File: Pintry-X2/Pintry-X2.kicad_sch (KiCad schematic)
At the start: 0 parts

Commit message: Bunch of shit done, probably should commit
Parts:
- added FID1, FID3, FID5: FiducialTop, symbol Mechanical:Fiducial
- added FID2, FID4, FID6: FiducialBot, symbol Mechanical:Fiducial
- added H1, H2, H3, H4: M3 MountingHole, symbol Mechanical:MountingHole
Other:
- sheet CM4 renamed CM4-ETH-GPIO
- added sheet CM4-USB-PCIe (CM4-USB-PCIe.kicad_sch)
- added sheet PCIe to SATA (PCIe_To_SATA.kicad_sch)
- added sheet Power Supply (PowerSupply.kicad_sch)
- sheet CM4-ETH-GPIO: file CM4.kicad_sch -> CM4-ETH-GPIO.kicad_sch
- note added: "PCIe RX/TX from Host perspective"
- company: (none) -> www.cezarchirila.com
- title: (none) -> Pintry X2

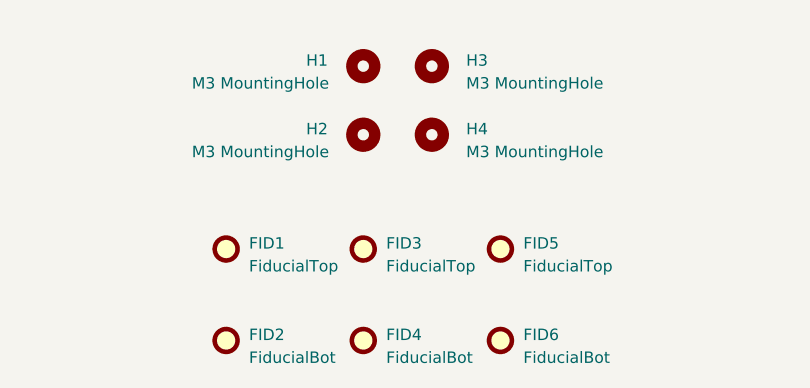
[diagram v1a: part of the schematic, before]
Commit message: Cleaned up schematic
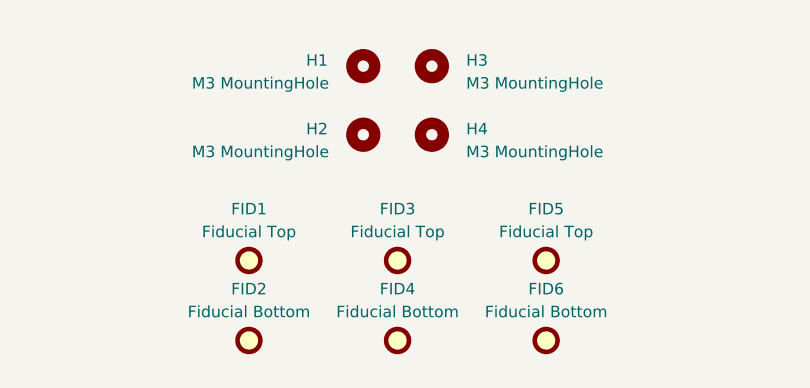
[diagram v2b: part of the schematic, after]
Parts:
- FID1, FID3, FID5: value FiducialTop -> Fiducial Top; footprint (none) -> Fiducial:Fiducial_1mm_Mask2mm; now in the parts list
- FID2, FID4, FID6: value FiducialBot -> Fiducial Bottom; footprint (none) -> Fiducial:Fiducial_1mm_Mask2mm; now in the parts list
- H1, H2, H3, H4: footprint (none) -> MountingHole:MountingHole_3.2mm_M3

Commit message: Finished Shematic. Starting PCB
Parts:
- H1, H2, H3, H4: footprint MountingHole:MountingHole_3.2mm_M3 -> PintryParts-Footprints:MountingHole_3.2mm_M3

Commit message: PCB Routing Complete - needs review
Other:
- sheet CM4-ETH-GPIO ports: added ~{RPIBOOT}; removed none
- sheet CM4-USB-PCIe ports: added ~{PCIe_RST}, ~{RPIBOOT}; removed ~PCIe_RST
- sheet PCIe to SATA ports: added ~{PCIe_RST}; removed ~PCIe_RST
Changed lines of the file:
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@@
-(kicad_sch (version 20210406) (generator eeschema)
+(kicad_sch (version 20210621) (generator eeschema)
   (paper "A3")
   (title_block
@@
     (comment 9 "${DrawnBy}")
   )
+  (wire (pts (xy 139.7 119.38) (xy 152.4 119.38))
+    (stroke (width 0) (type default) (color 0 0 0 0))
+  )
   (wire (pts (xy 190.5 96.52) (xy 203.2 96.52))
     (stroke (width 0) (type solid) (color 0 0 0 0))
@@
       (effects (font (size 1.27 1.27)) (justify left top))
     )
+    (pin "~{RPIBOOT}" input (at 139.7 119.38 0)
+      (effects (font (size 1.27 1.27)) (justify right))
+    )
   )
   (sheet (at 152.4 88.9) (size 38.1 38.1) (fields_autoplaced)
@@
       (effects (font (size 1.27 1.27)) (justify left top))
     )
-    (pin "~PCIe_RST" output (at 190.5 96.52 0)
+    (pin "~{PCIe_RST}" output (at 190.5 96.52 0)
       (effects (font (size 1.27 1.27)) (justify right))
     )
@@
     (pin "PCIe_TX_P" output (at 190.5 116.84 0)
       (effects (font (size 1.27 1.27)) (justify right))
+    )
+    (pin "~{RPIBOOT}" output (at 152.4 119.38 180)
+      (effects (font (size 1.27 1.27)) (justify left))
     )
   )
@@
       (effects (font (size 1.27 1.27)) (justify left))
     )
-    (pin "~PCIe_RST" input (at 203.2 96.52 180)
+    (pin "~{PCIe_RST}" input (at 203.2 96.52 180)
       (effects (font (size 1.27 1.27)) (justify left))
     )
@@
       (reference "#PWR0144") (unit 1) (value "GND") (footprint "")
     )
+    (path "/43f16507-298f-4d98-bfaf-f1724bb94aba/9d0fe3a6-d02b-4920-9231-813081adfc8b"
+      (reference "#PWR0145") (unit 1) (value "GND") (footprint "")
+    )
     (path "/9b6e5347-f86e-4db9-bbf5-31af483a2407/5e55dc42-0089-47bf-9024-2334ea89628c"
       (reference "#PWR0146") (unit 1) (value "GND") (footprint "")
@@
       (reference "#PWR0154") (unit 1) (value "GND") (footprint "")
     )
-    (path "/43f16507-298f-4d98-bfaf-f1724bb94aba/791d2112-1af0-4cac-90c1-821c2089ea1d"
-      (reference "#PWR0155") (unit 1) (value "GND") (footprint "")
-    )
     (path "/43f16507-298f-4d98-bfaf-f1724bb94aba/8ffb6013-907a-415f-9140-e7469dfe0209"
       (reference "#PWR0156") (unit 1) (value "GND") (footprint "")
@@
       (reference "Q2") (unit 1) (value "BSS138PW") (footprint "Package_TO_SOT_SMD:SOT-323_SC-70")
     )
+    (path "/43f16507-298f-4d98-bfaf-f1724bb94aba/81596eb1-0436-4fd2-ad41-2e3aa5c836ef"
+      (reference "Q3") (unit 1) (value "BSS138PW") (footprint "Package_TO_SOT_SMD:SOT-323_SC-70")
+    )
     (path "/9b6e5347-f86e-4db9-bbf5-31af483a2407/de22381e-32d3-41cf-bf63-26066b0511fe"
-      (reference "Q5") (unit 1) (value "SIA483DJ") (footprint "Package_TO_SOT_SMD:Vishay_PowerPAK_SC70-6L_Single")
+      (reference "Q5") (unit 1) (value "SIA483DJ") (footprint "PintryParts-Footprints:Vishay_PowerPAK_SC70-6L_Single")
     )
     (path "/9b6e5347-f86e-4db9-bbf5-31af483a2407/28421447-7a88-445b-abbf-05f73eb42385"
@@
     )
     (path "/9b6e5347-f86e-4db9-bbf5-31af483a2407/d3b4a547-7eca-4eee-b20e-40fe88c2e1c0"
-      (reference "Q7") (unit 1) (value "SIA483DJ") (footprint "Package_TO_SOT_SMD:Vishay_PowerPAK_SC70-6L_Single")
+      (reference "Q7") (unit 1) (value "SIA483DJ") (footprint "PintryParts-Footprints:Vishay_PowerPAK_SC70-6L_Single")
     )
     (path "/9d10082d-34aa-4b2a-aed1-f6a03e5ca555/359a6298-4ff1-4a7f-aed5-ce92ce328403"
@@
       (reference "R15") (unit 1) (value "100K") (footprint "PintryParts-Footprints:R_0402_1005Metric")
     )
+    (path "/43f16507-298f-4d98-bfaf-f1724bb94aba/672e95d7-1401-4782-b5cf-4656984e1abd"
+      (reference "R16") (unit 1) (value "4K7") (footprint "PintryParts-Footprints:R_0402_1005Metric")
+    )
     (path "/d684709a-a958-44ce-bda0-0bbe09272c17/ff52700d-8342-4346-a086-6f3401fcb1b4"
       (reference "R17") (unit 1) (value "4K7") (footprint "PintryParts-Footprints:R_0402_1005Metric")
@@
       (reference "R18") (unit 1) (value "4K7") (footprint "PintryParts-Footprints:R_0402_1005Metric")
     )
+    (path "/9d10082d-34aa-4b2a-aed1-f6a03e5ca555/6b228126-496c-42dc-b2d9-4dea7ae53083"
+      (reference "R19") (unit 1) (value "1K") (footprint "PintryParts-Footprints:R_0402_1005Metric")
+    )
+    (path "/9d10082d-34aa-4b2a-aed1-f6a03e5ca555/31137e12-48b1-4c0a-8c02-c20834998509"
+      (reference "R20") (unit 1) (value "1K") (footprint "PintryParts-Footprints:R_0402_1005Metric")
+    )
     (path "/d684709a-a958-44ce-bda0-0bbe09272c17/9cefef80-cbca-400d-9c9b-05546550af89"
       (reference "R21") (unit 1) (value "4K7") (footprint "PintryParts-Footprints:R_0402_1005Metric")
@@
     )
     (path "/9b6e5347-f86e-4db9-bbf5-31af483a2407/0882f70b-802c-4545-afe3-58c1fc910636"
-      (reference "TP1") (unit 1) (value "VIN") (footprint "TestPoint:TestPoint_Pad_D1.0mm")
+      (reference "TP1") (unit 1) (value "VIN") (footprint "PintryParts-Footprints:TestPoint_Pad_D1.0mm")
     )
     (path "/9b6e5347-f86e-4db9-bbf5-31af483a2407/f26086ec-723e-4c84-ab4c-4ea21b12643d"
-      (reference "TP2") (unit 1) (value "VCC") (footprint "TestPoint:TestPoint_Pad_D1.0mm")
+      (reference "TP2") (unit 1) (value "VCC") (footprint "PintryParts-Footprints:TestPoint_Pad_D1.0mm")
     )
     (path "/9b6e5347-f86e-4db9-bbf5-31af483a2407/8064058a-d19e-48ad-8198-501652b96543"
-      (reference "TP3") (unit 1) (value "VIN_RP") (footprint "TestPoint:TestPoint_Pad_D1.0mm")
+      (reference "TP3") (unit 1) (value "VIN_RP") (footprint "PintryParts-Footprints:TestPoint_Pad_D1.0mm")
     )
     (path "/9b6e5347-f86e-4db9-bbf5-31af483a2407/b4f89b4b-1bf6-4b5b-acbb-f37c37c96e6f"
-      (reference "TP4") (unit 1) (value "+5V") (footprint "TestPoint:TestPoint_Pad_D1.0mm")
+      (reference "TP4") (unit 1) (value "+5V") (footprint "PintryParts-Footprints:TestPoint_Pad_D1.0mm")
     )
     (path "/9b6e5347-f86e-4db9-bbf5-31af483a2407/2e24b85f-2f5e-4941-a948-77329a33f8fa"
-      (reference "TP5") (unit 1) (value "+12V") (footprint "TestPoint:TestPoint_Pad_D1.0mm")
+      (reference "TP5") (unit 1) (value "+12V") (footprint "PintryParts-Footprints:TestPoint_Pad_D1.0mm")
     )
     (path "/9b6e5347-f86e-4db9-bbf5-31af483a2407/83ab9e94-6dc3-42bd-ade7-a66fa1afb484"
-      (reference "TP6") (unit 1) (value "GND") (footprint "TestPoint:TestPoint_Pad_D1.0mm")
+      (reference "TP6") (unit 1) (value "GND") (footprint "PintryParts-Footprints:TestPoint_Pad_D1.0mm")
     )
     (path "/9d10082d-34aa-4b2a-aed1-f6a03e5ca555/5f06c418-35af-4a8b-8229-a1fb9d539fcb"
-      (reference "TP7") (unit 1) (value "RUN_PG") (footprint "TestPoint:TestPoint_Pad_D1.0mm")
+      (reference "TP7") (unit 1) (value "RUN_PG") (footprint "PintryParts-Footprints:TestPoint_Pad_D1.0mm")
     )
     (path "/9d10082d-34aa-4b2a-aed1-f6a03e5ca555/04199f63-e06c-4307-a8f2-2c85a7013a1a"
-      (reference "TP8") (unit 1) (value "GLOBAL_EN") (footprint "TestPoint:TestPoint_Pad_D1.0mm")
+      (reference "TP8") (unit 1) (value "GLOBAL_EN") (footprint "PintryParts-Footprints:TestPoint_Pad_D1.0mm")
     )
     (path "/9d10082d-34aa-4b2a-aed1-f6a03e5ca555/942e11b9-c098-48e4-b9a0-ea01936abccd"
-      (reference "TP9") (unit 1) (value "FAN1") (footprint "TestPoint:TestPoint_Pad_D1.0mm")
+      (reference "TP9") (unit 1) (value "FAN1") (footprint "PintryParts-Footprints:TestPoint_Pad_D1.0mm")
     )
     (path "/9d10082d-34aa-4b2a-aed1-f6a03e5ca555/d5de8427-e722-4a00-9973-3fee3858dae5"
-      (reference "TP10") (unit 1) (value "FAN0") (footprint "TestPoint:TestPoint_Pad_D1.0mm")
+      (reference "TP10") (unit 1) (value "FAN0") (footprint "PintryParts-Footprints:TestPoint_Pad_D1.0mm")
     )
     (path "/d684709a-a958-44ce-bda0-0bbe09272c17/b6d8b293-1883-4d02-93bf-609d602728ca"
-      (reference "TP11") (unit 1) (value "+1V2") (footprint "TestPoint:TestPoint_Pad_D1.0mm")
+      (reference "TP11") (unit 1) (value "+1V2") (footprint "PintryParts-Footprints:TestPoint_Pad_D1.0mm")
     )
     (path "/43f16507-298f-4d98-bfaf-f1724bb94aba/fbba102e-6543-4d65-941e-5581190f8529"
-      (reference "TP14") (unit 1) (value "VUSB") (footprint "TestPoint:TestPoint_Pad_D1.0mm")
+      (reference "TP14") (unit 1) (value "VUSB") (footprint "PintryParts-Footprints:TestPoint_Pad_D1.0mm")
     )
     (path "/9b6e5347-f86e-4db9-bbf5-31af483a2407/bdb5647d-0615-4715-bb8e-a987dc84acec"
-      (reference "TP15") (unit 1) (value "GND") (footprint "TestPoint:TestPoint_Pad_D1.0mm")
+      (reference "TP15") (unit 1) (value "GND") (footprint "PintryParts-Footprints:TestPoint_Pad_D1.0mm")
     )
     (path "/9b6e5347-f86e-4db9-bbf5-31af483a2407/8aaeecbf-c658-4df9-8c68-6792c6dc1446"
-      (reference "TP16") (unit 1) (value "GND") (footprint "TestPoint:TestPoint_Pad_D1.0mm")
+      (reference "TP16") (unit 1) (value "GND") (footprint "PintryParts-Footprints:TestPoint_Pad_D1.0mm")
     )
     (path "/9b6e5347-f86e-4db9-bbf5-31af483a2407/59f4fbe6-270b-4071-926d-f9afce828fb6"
-      (reference "TP17") (unit 1) (value "GND") (footprint "TestPoint:TestPoint_Pad_D1.0mm")
+      (reference "TP17") (unit 1) (value "GND") (footprint "PintryParts-Footprints:TestPoint_Pad_D1.0mm")
     )
     (path "/9d10082d-34aa-4b2a-aed1-f6a03e5ca555/f3b7861f-1ccf-4504-af2b-07baaa0f74c4"
-      (reference "TP18") (unit 1) (value "3V3") (footprint "TestPoint:TestPoint_Pad_D1.0mm")
+      (reference "TP18") (unit 1) (value "3V3") (footprint "PintryParts-Footprints:TestPoint_Pad_D1.0mm")
     )
     (path "/9d10082d-34aa-4b2a-aed1-f6a03e5ca555/0fed7a6b-5f61-431f-abc4-a9bf842b3eee"

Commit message: Updated to Rev 1.1. Added interactive HTML
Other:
- note added: "Changelog:"
- note added: "V1.0 - Initial Release"
- note added: "V1.1 - Changed R14 to 1K. Fixed SST25VF512A footprint. Fixed Y1 pinout."
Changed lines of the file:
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@@
     (stroke (width 0) (type solid) (color 0 0 0 0))
+  )
+  (text "Changelog:\n" (at 38.1 238.76 0)
+    (effects (font (size 1.8 1.8) (thickness 0.254) bold) (justify left bottom))
+  )
+  (text "V1.0 - Initial Release\n" (at 38.1 242.57 0)
+    (effects (font (size 1.8 1.8)) (justify left bottom))
+  )
+  (text "V1.1 - Changed R14 to 1K. Fixed SST25VF512A footprint. Fixed Y1 pinout.\n\n\n\n "
+    (at 38.1 257.81 0)
+    (effects (font (size 1.8 1.8)) (justify left bottom))
   )
   (text "PCIe RX/TX from Host perspective" (at 179.07 133.35 0)
@@
     )
     (path "/d684709a-a958-44ce-bda0-0bbe09272c17/4b139e0e-b32a-4583-81cf-842901f3e977"
-      (reference "R14") (unit 1) (value "4K7") (footprint "PintryParts-Footprints:R_0402_1005Metric")
+      (reference "R14") (unit 1) (value "1K") (footprint "PintryParts-Footprints:R_0402_1005Metric")
     )
     (path "/9d10082d-34aa-4b2a-aed1-f6a03e5ca555/9740a87c-eb70-42e8-8352-c46b996b0405"
@@
     )
     (path "/d684709a-a958-44ce-bda0-0bbe09272c17/0d7ef888-f0d3-4c0a-9db1-a1092ada64a7"
-      (reference "U10") (unit 1) (value "SST25VF512A") (footprint "Package_SO:SOIC-8_5.275x5.275mm_P1.27mm")
+      (reference "U10") (unit 1) (value "SST25VF512A") (footprint "Package_SO:SOIC-8_3.9x4.9mm_P1.27mm")
     )
     (path "/d684709a-a958-44ce-bda0-0bbe09272c17/967707d1-cc15-44c4-ad21-402dd30edde5"

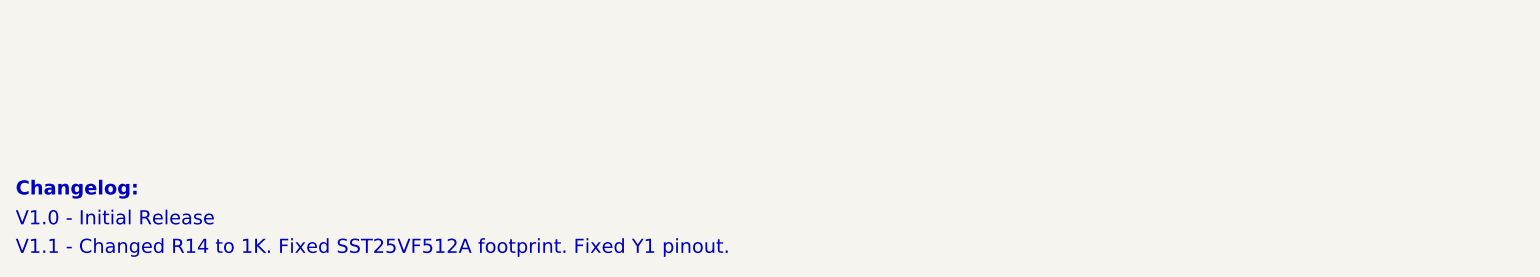
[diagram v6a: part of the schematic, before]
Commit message: Fixed ON/OFF Button
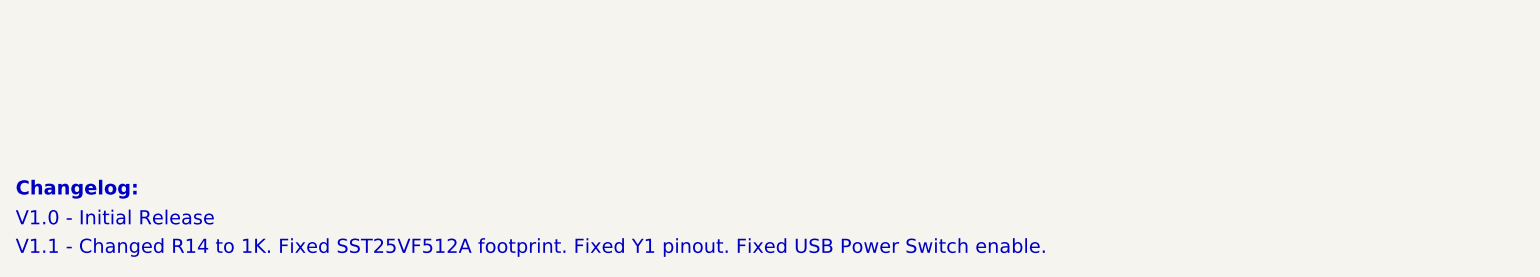
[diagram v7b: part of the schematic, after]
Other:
- note added: "V1.1 - Changed R14 to 1K. Fixed SST25VF512A footprint. Fixed Y1 pinout. Fixed USB Power Switch enable."
- note removed: "V1.1 - Changed R14 to 1K. Fixed SST25VF512A footprint. Fixed Y1 pinout."
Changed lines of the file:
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@@
     (effects (font (size 1.8 1.8)) (justify left bottom))
   )
-  (text "V1.1 - Changed R14 to 1K. Fixed SST25VF512A footprint. Fixed Y1 pinout.\n\n\n\n "
+  (text "V1.1 - Changed R14 to 1K. Fixed SST25VF512A footprint. Fixed Y1 pinout. Fixed USB Power Switch enable. \n\n\n\n "
     (at 38.1 257.81 0)
     (effects (font (size 1.8 1.8)) (justify left bottom))
@@
       (reference "#PWR033") (unit 1) (value "+3.3V") (footprint "")
     )
-    (path "/9d10082d-34aa-4b2a-aed1-f6a03e5ca555/62d0e961-8513-496f-8a5d-418bb6ab73c1"
-      (reference "#PWR034") (unit 1) (value "+3.3V") (footprint "")
+    (path "/9d10082d-34aa-4b2a-aed1-f6a03e5ca555/04ab7149-7bbc-4256-9047-d982054a754c"
+      (reference "#PWR034") (unit 1) (value "+5V") (footprint "")
     )
     (path "/43f16507-298f-4d98-bfaf-f1724bb94aba/dbbe10b1-a04f-447b-9b52-05ad854ee7cb"
@@
       (reference "#PWR074") (unit 1) (value "GND") (footprint "")
     )
-    (path "/9d10082d-34aa-4b2a-aed1-f6a03e5ca555/79648b23-c26d-467d-9176-8ba48718babe"
+    (path "/9d10082d-34aa-4b2a-aed1-f6a03e5ca555/e9b55565-de45-4b28-a951-034691780f85"
       (reference "#PWR075") (unit 1) (value "GND") (footprint "")
     )
@@
       (reference "D6") (unit 1) (value "D3V3M1U259-7") (footprint "Diode_SMD:D_SOD-923")
     )
-    (path "/9d10082d-34aa-4b2a-aed1-f6a03e5ca555/52ebbd65-f42c-4ca1-bcff-f69e932068e7"
-      (reference "D7") (unit 1) (value "D3V3M1U259-7") (footprint "Diode_SMD:D_SOD-923")
+    (path "/9d10082d-34aa-4b2a-aed1-f6a03e5ca555/a0f6f20a-b607-4c46-8091-4483967c9f9a"
+      (reference "D7") (unit 1) (value "DF2S6.2FS,L3M") (footprint "Diode_SMD:D_SOD-923")
     )
     (path "/9d10082d-34aa-4b2a-aed1-f6a03e5ca555/9416faeb-54cd-4a5d-9519-11badceae2fc"
@@
       (reference "R35") (unit 1) (value "100k") (footprint "PintryParts-Footprints:R_0402_1005Metric")
     )
+    (path "/9d10082d-34aa-4b2a-aed1-f6a03e5ca555/efb4912c-2031-4dee-b422-66650b5ac057"
+      (reference "R36") (unit 1) (value "100K") (footprint "PintryParts-Footprints:R_0402_1005Metric")
+    )
     (path "/9d10082d-34aa-4b2a-aed1-f6a03e5ca555/6f1202d7-2506-4e0e-b360-a3da4e4649bc"
